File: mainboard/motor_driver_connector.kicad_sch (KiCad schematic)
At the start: 1 part, among them J4 CON_CONNAXIO_MOTOR_DRIVER

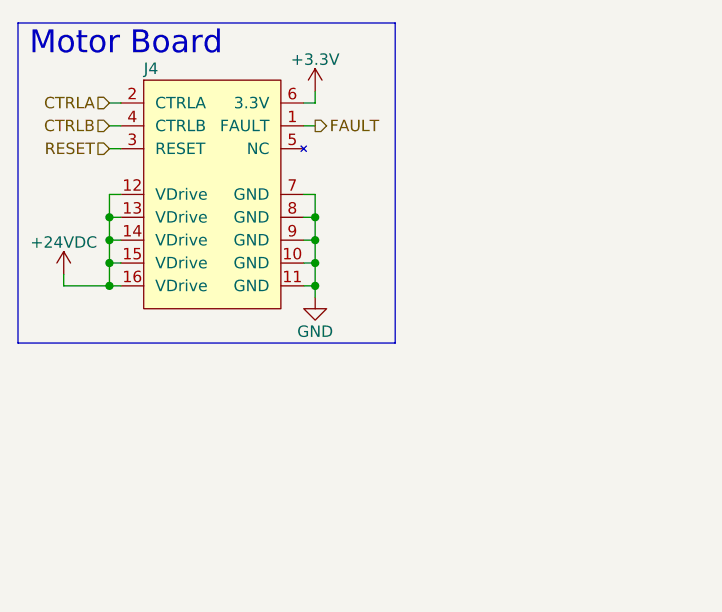
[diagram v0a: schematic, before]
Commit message: Inverted motor controls for open-drain operation and manual switch override compatibility
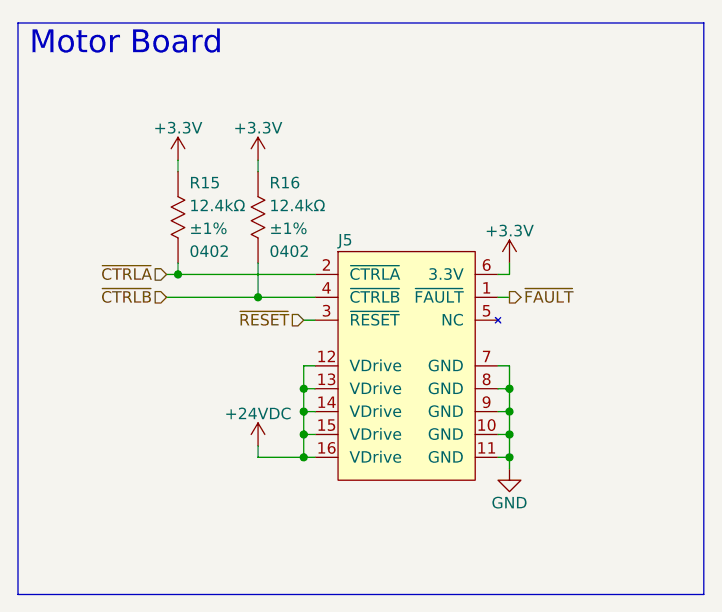
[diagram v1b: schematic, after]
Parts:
- added R15, R16: RES_12.4KΩ_1%_0402, connaxio-resistors:RES_0402_1005M, symbol connaxio-resistors:RES_12.4KΩ_1%_0402
- renumbered J4 to J5
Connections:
- net +3.3V: now also R15.1, R16.1
- net CTRLA renamed ~{CTRLA}
- net ~{CTRLA}: now also R15.2
- net CTRLB renamed ~{CTRLB}
- net ~{CTRLB}: now also R16.2
- net FAULT renamed ~{FAULT}
- net RESET renamed ~{RESET}
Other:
- moved on the sheet: J5

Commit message: Position drive rmodules, choose enclosure, shape PCB
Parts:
- renumbered R15 to R14, R16 to R15
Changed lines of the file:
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@@
   (symbol (lib_id "connaxio-power:+24VDC") (at 41.91 62.23 0) (mirror y) (unit 1)
     (in_bom yes) (on_board yes)
-    (property "Reference" "#PWR045" (id 0) (at 41.91 66.04 0)
+    (property "Reference" "#PWR044" (id 0) (at 41.91 66.04 0)
       (effects (font (size 1.27 1.27)) hide)
     )
@@
   (symbol (lib_id "power:+3.3V") (at 41.91 30.48 0) (mirror y) (unit 1)
     (in_bom yes) (on_board yes)
-    (property "Reference" "#PWR043" (id 0) (at 41.91 34.29 0)
+    (property "Reference" "#PWR042" (id 0) (at 41.91 34.29 0)
       (effects (font (size 1.27 1.27)) hide)
     )
@@
   (symbol (lib_id "connaxio-resistors:RES_12.4KΩ_1%_0402") (at 33.02 36.83 0) (unit 1)
     (in_bom yes) (on_board yes)
-    (property "Reference" "R15" (id 0) (at 34.29 33.02 0)
+    (property "Reference" "R14" (id 0) (at 34.29 33.02 0)
       (effects (font (size 1.27 1.27)) (justify left))
     )
@@
   (symbol (lib_id "connaxio-resistors:RES_12.4KΩ_1%_0402") (at 41.91 36.83 0) (unit 1)
     (in_bom yes) (on_board yes)
-    (property "Reference" "R16" (id 0) (at 43.18 33.02 0)
+    (property "Reference" "R15" (id 0) (at 43.18 33.02 0)
       (effects (font (size 1.27 1.27)) (justify left))
     )
@@
   (symbol (lib_id "power:+3.3V") (at 69.85 41.91 0) (mirror y) (unit 1)
     (in_bom yes) (on_board yes)
-    (property "Reference" "#PWR044" (id 0) (at 69.85 45.72 0)
+    (property "Reference" "#PWR043" (id 0) (at 69.85 45.72 0)
       (effects (font (size 1.27 1.27)) hide)
     )
@@
   (symbol (lib_id "power:GND") (at 69.85 64.77 0) (mirror y) (unit 1)
     (in_bom yes) (on_board yes)
-    (property "Reference" "#PWR046" (id 0) (at 69.85 71.12 0)
+    (property "Reference" "#PWR045" (id 0) (at 69.85 71.12 0)
       (effects (font (size 1.27 1.27)) hide)
     )
@@
   (symbol (lib_id "power:+3.3V") (at 33.02 30.48 0) (mirror y) (unit 1)
     (in_bom yes) (on_board yes)
-    (property "Reference" "#PWR042" (id 0) (at 33.02 34.29 0)
-      (effects (font (size 1.27 1.27)) hide)
-    )
+    (property "Reference" "#PWR041" (id 0) (at 33.02 34.29 0)
+      (effects (font (size 1.27 1.27)) hide)
+    )

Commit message: Routing mainboard
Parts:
- renumbered J5 to J6
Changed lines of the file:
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@@
   (symbol (lib_id "connaxio-power:+24VDC") (at 41.91 62.23 0) (mirror y) (unit 1)
     (in_bom yes) (on_board yes)
-    (property "Reference" "#PWR044" (id 0) (at 41.91 66.04 0)
+    (property "Reference" "#PWR048" (id 0) (at 41.91 66.04 0)
       (effects (font (size 1.27 1.27)) hide)
     )
@@
   (symbol (lib_id "power:+3.3V") (at 41.91 30.48 0) (mirror y) (unit 1)
     (in_bom yes) (on_board yes)
-    (property "Reference" "#PWR042" (id 0) (at 41.91 34.29 0)
+    (property "Reference" "#PWR046" (id 0) (at 41.91 34.29 0)
       (effects (font (size 1.27 1.27)) hide)
     )
@@
   (symbol (lib_id "power:+3.3V") (at 69.85 41.91 0) (mirror y) (unit 1)
     (in_bom yes) (on_board yes)
-    (property "Reference" "#PWR043" (id 0) (at 69.85 45.72 0)
+    (property "Reference" "#PWR047" (id 0) (at 69.85 45.72 0)
       (effects (font (size 1.27 1.27)) hide)
     )
@@
   (symbol (lib_id "power:GND") (at 69.85 64.77 0) (mirror y) (unit 1)
     (in_bom yes) (on_board yes)
-    (property "Reference" "#PWR045" (id 0) (at 69.85 71.12 0)
+    (property "Reference" "#PWR049" (id 0) (at 69.85 71.12 0)
       (effects (font (size 1.27 1.27)) hide)
     )
@@
   (symbol (lib_id "connaxio-connectors:CON_CONNAXIO_MOTOR_DRIVER") (at 50.8 40.64 0) (unit 1)
     (in_bom yes) (on_board yes)
-    (property "Reference" "J5" (id 0) (at 50.8 39.37 0)
+    (property "Reference" "J6" (id 0) (at 50.8 39.37 0)
       (effects (font (size 1.27 1.27)) (justify left))
     )
@@
   (symbol (lib_id "power:+3.3V") (at 33.02 30.48 0) (mirror y) (unit 1)
     (in_bom yes) (on_board yes)
-    (property "Reference" "#PWR041" (id 0) (at 33.02 34.29 0)
-      (effects (font (size 1.27 1.27)) hide)
-    )
+    (property "Reference" "#PWR045" (id 0) (at 33.02 34.29 0)
+      (effects (font (size 1.27 1.27)) hide)
+    )

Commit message: Add LEDs, fix NMOS, Add logos and infos on PCBs.
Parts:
- renumbered R14 to R17, R15 to R18
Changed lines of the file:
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@@
   (symbol (lib_id "connaxio-power:+24VDC") (at 41.91 62.23 0) (mirror y) (unit 1)
     (in_bom yes) (on_board yes)
-    (property "Reference" "#PWR052" (id 0) (at 41.91 66.04 0)
+    (property "Reference" "#PWR058" (id 0) (at 41.91 66.04 0)
       (effects (font (size 1.27 1.27)) hide)
     )
@@
   (symbol (lib_id "power:+3.3V") (at 41.91 30.48 0) (mirror y) (unit 1)
     (in_bom yes) (on_board yes)
-    (property "Reference" "#PWR050" (id 0) (at 41.91 34.29 0)
+    (property "Reference" "#PWR056" (id 0) (at 41.91 34.29 0)
       (effects (font (size 1.27 1.27)) hide)
     )
@@
   (symbol (lib_id "connaxio-resistors:RES_12.4KΩ_1%_0402") (at 33.02 36.83 0) (unit 1)
     (in_bom yes) (on_board yes)
-    (property "Reference" "R14" (id 0) (at 34.29 33.02 0)
+    (property "Reference" "R17" (id 0) (at 34.29 33.02 0)
       (effects (font (size 1.27 1.27)) (justify left))
     )
@@
   (symbol (lib_id "connaxio-resistors:RES_12.4KΩ_1%_0402") (at 41.91 36.83 0) (unit 1)
     (in_bom yes) (on_board yes)
-    (property "Reference" "R15" (id 0) (at 43.18 33.02 0)
+    (property "Reference" "R18" (id 0) (at 43.18 33.02 0)
       (effects (font (size 1.27 1.27)) (justify left))
     )
@@
   (symbol (lib_id "power:+3.3V") (at 69.85 41.91 0) (mirror y) (unit 1)
     (in_bom yes) (on_board yes)
-    (property "Reference" "#PWR051" (id 0) (at 69.85 45.72 0)
+    (property "Reference" "#PWR057" (id 0) (at 69.85 45.72 0)
       (effects (font (size 1.27 1.27)) hide)
     )
@@
   (symbol (lib_id "power:GND") (at 69.85 64.77 0) (mirror y) (unit 1)
     (in_bom yes) (on_board yes)
-    (property "Reference" "#PWR053" (id 0) (at 69.85 71.12 0)
+    (property "Reference" "#PWR059" (id 0) (at 69.85 71.12 0)
       (effects (font (size 1.27 1.27)) hide)
     )
@@
   (symbol (lib_id "power:+3.3V") (at 33.02 30.48 0) (mirror y) (unit 1)
     (in_bom yes) (on_board yes)
-    (property "Reference" "#PWR049" (id 0) (at 33.02 34.29 0)
-      (effects (font (size 1.27 1.27)) hide)
-    )
+    (property "Reference" "#PWR055" (id 0) (at 33.02 34.29 0)
+      (effects (font (size 1.27 1.27)) hide)
+    )

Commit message: Invert connectors (male/female) Replace TH connectors with SMD ones on mainboard Add 555 timer on simple-switch to generate 60 Hz Add jumper on simple-switch to select AC Add series I2C resistors on mainboard from mikroBUS socket
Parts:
- renumbered R17 to R19, R18 to R20
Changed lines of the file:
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@@
   (symbol (lib_id "connaxio-resistors:RES_12.4KΩ_1%_0402") (at 33.02 36.83 0) (unit 1)
     (in_bom yes) (on_board yes)
-    (property "Reference" "R17" (id 0) (at 34.29 33.02 0)
+    (property "Reference" "R19" (id 0) (at 34.29 33.02 0)
       (effects (font (size 1.27 1.27)) (justify left))
     )
@@
   (symbol (lib_id "connaxio-resistors:RES_12.4KΩ_1%_0402") (at 41.91 36.83 0) (unit 1)
     (in_bom yes) (on_board yes)
-    (property "Reference" "R18" (id 0) (at 43.18 33.02 0)
+    (property "Reference" "R20" (id 0) (at 43.18 33.02 0)
       (effects (font (size 1.27 1.27)) (justify left))
     )

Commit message: Add onboard temperature sensor Add connector for Analog / 1-wire / PWM sensor
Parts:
- renumbered J6 to J7, R19 to R21, R20 to R22
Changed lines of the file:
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@@
   (symbol (lib_id "connaxio-power:+24VDC") (at 41.91 62.23 0) (mirror y) (unit 1)
     (in_bom yes) (on_board yes)
-    (property "Reference" "#PWR058" (id 0) (at 41.91 66.04 0)
+    (property "Reference" "#PWR064" (id 0) (at 41.91 66.04 0)
       (effects (font (size 1.27 1.27)) hide)
     )
@@
   (symbol (lib_id "power:+3.3V") (at 41.91 30.48 0) (mirror y) (unit 1)
     (in_bom yes) (on_board yes)
-    (property "Reference" "#PWR056" (id 0) (at 41.91 34.29 0)
+    (property "Reference" "#PWR062" (id 0) (at 41.91 34.29 0)
       (effects (font (size 1.27 1.27)) hide)
     )
@@
   (symbol (lib_id "connaxio-resistors:RES_12.4KΩ_1%_0402") (at 33.02 36.83 0) (unit 1)
     (in_bom yes) (on_board yes)
-    (property "Reference" "R19" (id 0) (at 34.29 33.02 0)
+    (property "Reference" "R21" (id 0) (at 34.29 33.02 0)
       (effects (font (size 1.27 1.27)) (justify left))
     )
@@
   (symbol (lib_id "connaxio-resistors:RES_12.4KΩ_1%_0402") (at 41.91 36.83 0) (unit 1)
     (in_bom yes) (on_board yes)
-    (property "Reference" "R20" (id 0) (at 43.18 33.02 0)
+    (property "Reference" "R22" (id 0) (at 43.18 33.02 0)
       (effects (font (size 1.27 1.27)) (justify left))
     )
@@
   (symbol (lib_id "power:+3.3V") (at 69.85 41.91 0) (mirror y) (unit 1)
     (in_bom yes) (on_board yes)
-    (property "Reference" "#PWR057" (id 0) (at 69.85 45.72 0)
+    (property "Reference" "#PWR063" (id 0) (at 69.85 45.72 0)
       (effects (font (size 1.27 1.27)) hide)
     )
@@
   (symbol (lib_id "power:GND") (at 69.85 64.77 0) (mirror y) (unit 1)
     (in_bom yes) (on_board yes)
-    (property "Reference" "#PWR059" (id 0) (at 69.85 71.12 0)
+    (property "Reference" "#PWR065" (id 0) (at 69.85 71.12 0)
       (effects (font (size 1.27 1.27)) hide)
     )
@@
   (symbol (lib_id "connaxio-connectors:CON_CONNAXIO_MOTOR_DRIVER") (at 50.8 40.64 0) (unit 1)
     (in_bom yes) (on_board yes)
-    (property "Reference" "J6" (id 0) (at 50.8 39.37 0)
+    (property "Reference" "J7" (id 0) (at 50.8 39.37 0)
       (effects (font (size 1.27 1.27)) (justify left))
     )
@@
   (symbol (lib_id "power:+3.3V") (at 33.02 30.48 0) (mirror y) (unit 1)
     (in_bom yes) (on_board yes)
-    (property "Reference" "#PWR055" (id 0) (at 33.02 34.29 0)
-      (effects (font (size 1.27 1.27)) hide)
-    )
+    (property "Reference" "#PWR061" (id 0) (at 33.02 34.29 0)
+      (effects (font (size 1.27 1.27)) hide)
+    )

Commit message: Add 4 extra IOs (SVG connectors)
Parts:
- renumbered J7 to J10, R21 to R24, R22 to R25
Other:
- company: (none) -> ${company}
- title: (none) -> ${title}
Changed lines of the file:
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@@
 (kicad_sch (version 20211123) (generator eeschema)
   (paper "A4")
+  (title_block
+    (title "${title}")
+    (date "${year}-${month}-${day}")
+    (rev "${rev}")
+    (company "${company}")
+    (comment 1 "${author}")
+  )
   (junction (at 69.85 63.5) (diameter 0) (color 0 0 0 0)
   )
@@
   (symbol (lib_id "connaxio-power:+24VDC") (at 41.91 62.23 0) (mirror y) (unit 1)
     (in_bom yes) (on_board yes)
-    (property "Reference" "#PWR064" (id 0) (at 41.91 66.04 0)
+    (property "Reference" "#PWR069" (id 0) (at 41.91 66.04 0)
       (effects (font (size 1.27 1.27)) hide)
     )
@@
   (symbol (lib_id "power:+3.3V") (at 41.91 30.48 0) (mirror y) (unit 1)
     (in_bom yes) (on_board yes)
-    (property "Reference" "#PWR062" (id 0) (at 41.91 34.29 0)
+    (property "Reference" "#PWR067" (id 0) (at 41.91 34.29 0)
       (effects (font (size 1.27 1.27)) hide)
     )
@@
   (symbol (lib_id "connaxio-resistors:RES_12.4KΩ_1%_0402") (at 33.02 36.83 0) (unit 1)
     (in_bom yes) (on_board yes)
-    (property "Reference" "R21" (id 0) (at 34.29 33.02 0)
+    (property "Reference" "R24" (id 0) (at 34.29 33.02 0)
       (effects (font (size 1.27 1.27)) (justify left))
     )
@@
   (symbol (lib_id "connaxio-resistors:RES_12.4KΩ_1%_0402") (at 41.91 36.83 0) (unit 1)
     (in_bom yes) (on_board yes)
-    (property "Reference" "R22" (id 0) (at 43.18 33.02 0)
+    (property "Reference" "R25" (id 0) (at 43.18 33.02 0)
       (effects (font (size 1.27 1.27)) (justify left))
     )
@@
   (symbol (lib_id "power:+3.3V") (at 69.85 41.91 0) (mirror y) (unit 1)
     (in_bom yes) (on_board yes)
-    (property "Reference" "#PWR063" (id 0) (at 69.85 45.72 0)
+    (property "Reference" "#PWR068" (id 0) (at 69.85 45.72 0)
       (effects (font (size 1.27 1.27)) hide)
     )
@@
   (symbol (lib_id "power:GND") (at 69.85 64.77 0) (mirror y) (unit 1)
     (in_bom yes) (on_board yes)
-    (property "Reference" "#PWR065" (id 0) (at 69.85 71.12 0)
+    (property "Reference" "#PWR070" (id 0) (at 69.85 71.12 0)
       (effects (font (size 1.27 1.27)) hide)
     )
@@
   (symbol (lib_id "connaxio-connectors:CON_CONNAXIO_MOTOR_DRIVER") (at 50.8 40.64 0) (unit 1)
     (in_bom yes) (on_board yes)
-    (property "Reference" "J7" (id 0) (at 50.8 39.37 0)
+    (property "Reference" "J10" (id 0) (at 50.8 39.37 0)
       (effects (font (size 1.27 1.27)) (justify left))
     )
@@
   (symbol (lib_id "power:+3.3V") (at 33.02 30.48 0) (mirror y) (unit 1)
     (in_bom yes) (on_board yes)
-    (property "Reference" "#PWR061" (id 0) (at 33.02 34.29 0)
-      (effects (font (size 1.27 1.27)) hide)
-    )
+    (property "Reference" "#PWR066" (id 0) (at 33.02 34.29 0)
+      (effects (font (size 1.27 1.27)) hide)
+    )
